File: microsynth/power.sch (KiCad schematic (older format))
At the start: 3 parts, among them J2 Conn_01x03_Male, J3 Conn_01x04_Male, J4 Conn_01x04_Male

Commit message: Add VCO2 on/off toggle, faceplace 3d, and new faceplate version
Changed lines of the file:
@@
 Wire Wire Line
 	4900 1500 4900 1350
-Text GLabel 5900 2900 2    50   BiDi ~ 0
+Text GLabel 5900 2600 2    50   BiDi ~ 0
 TRIG_IN_TO_SEQ_SKT
 Text GLabel 5900 2700 2    50   BiDi ~ 0
 VOUT_TO_SEQ_SKT
+Text GLabel 5900 2900 2    50   BiDi ~ 0
+VIN_TO_SEQ_SKT
 Text GLabel 5900 2800 2    50   BiDi ~ 0
-VIN_TO_SEQ_SKT
-Text GLabel 5900 2600 2    50   BiDi ~ 0
 TRIG_OUT_TO_SEQ_SKT
 Connection ~ 2250 1350

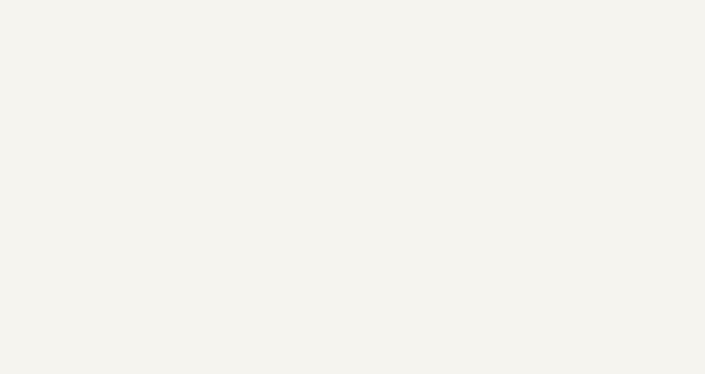
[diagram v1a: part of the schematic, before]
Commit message: Proper mounting holes
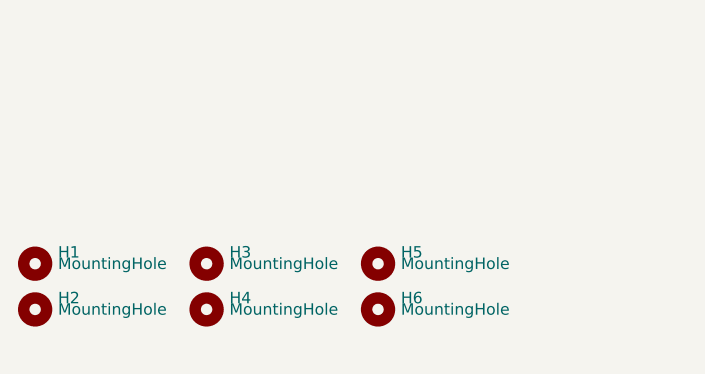
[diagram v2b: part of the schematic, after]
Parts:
- added H1, H2, H3, H4, H5, H6: MountingHole, MountingHole:MountingHole_3.2mm_M3, symbol Mechanical:MountingHole
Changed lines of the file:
@@
 Text GLabel 5900 3000 2    50   Input ~ 0
 VIN_FROM_SEQ
+$Comp
+L Mechanical:MountingHole H1
+U 1 1 5EBE889F
+P 1250 3300
+F 0 "H1" H 1350 3350 50  0000 L CNN
+F 1 "MountingHole" H 1350 3300 50  0000 L CNN
+F 2 "MountingHole:MountingHole_3.2mm_M3" H 1250 3300 50  0001 C CNN
+F 3 "~" H 1250 3300 50  0001 C CNN
+	1    1250 3300
+	1    0    0    -1
+$EndComp
+$Comp
+L Mechanical:MountingHole H2
+U 1 1 5EBEB2B9
+P 1250 3500
+F 0 "H2" H 1350 3550 50  0000 L CNN
+F 1 "MountingHole" H 1350 3500 50  0000 L CNN
+F 2 "MountingHole:MountingHole_3.2mm_M3" H 1250 3500 50  0001 C CNN
+F 3 "~" H 1250 3500 50  0001 C CNN
+	1    1250 3500
+	1    0    0    -1
+$EndComp
+$Comp
+L Mechanical:MountingHole H3
+U 1 1 5EBEC236
+P 2000 3300
+F 0 "H3" H 2100 3350 50  0000 L CNN
+F 1 "MountingHole" H 2100 3300 50  0000 L CNN
+F 2 "MountingHole:MountingHole_3.2mm_M3" H 2000 3300 50  0001 C CNN
+F 3 "~" H 2000 3300 50  0001 C CNN
+	1    2000 3300
+	1    0    0    -1
+$EndComp
+$Comp
+L Mechanical:MountingHole H4
+U 1 1 5EBEC23C
+P 2000 3500
+F 0 "H4" H 2100 3550 50  0000 L CNN
+F 1 "MountingHole" H 2100 3500 50  0000 L CNN
+F 2 "MountingHole:MountingHole_3.2mm_M3" H 2000 3500 50  0001 C CNN
+F 3 "~" H 2000 3500 50  0001 C CNN
+	1    2000 3500
+	1    0    0    -1
+$EndComp
+$Comp
+L Mechanical:MountingHole H5
+U 1 1 5EBECF2A
+P 2750 3300
+F 0 "H5" H 2850 3350 50  0000 L CNN
+F 1 "MountingHole" H 2850 3300 50  0000 L CNN
+F 2 "MountingHole:MountingHole_3.2mm_M3" H 2750 3300 50  0001 C CNN
+F 3 "~" H 2750 3300 50  0001 C CNN
+	1    2750 3300
+	1    0    0    -1
+$EndComp
+$Comp
+L Mechanical:MountingHole H6
+U 1 1 5EBECF30
+P 2750 3500
+F 0 "H6" H 2850 3550 50  0000 L CNN
+F 1 "MountingHole" H 2850 3500 50  0000 L CNN
+F 2 "MountingHole:MountingHole_3.2mm_M3" H 2750 3500 50  0001 C CNN
+F 3 "~" H 2750 3500 50  0001 C CNN
+	1    2750 3500
+	1    0    0    -1
+$EndComp
 $EndSCHEMATC

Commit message: Replace DP3T footprint, proper wire pads
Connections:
- net labels removed: +15V, -15V
- wire segments 10 -> 6
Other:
- moved on the sheet: J2
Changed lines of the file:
@@
 $EndDescr
-$Comp
-L power:+15V #PWR?
-U 1 1 5E05ECA4
-P 2500 1350
-F 0 "#PWR?" H 2500 1200 50  0001 C CNN
-F 1 "+15V" H 2515 1523 50  0000 C CNN
-F 2 "" H 2500 1350 50  0001 C CNN
-F 3 "" H 2500 1350 50  0001 C CNN
-	1    2500 1350
-	1    0    0    -1
-$EndComp
-$Comp
-L power:-15V #PWR?
-U 1 1 5E05F00D
-P 5450 1350
-F 0 "#PWR?" H 5450 1450 50  0001 C CNN
-F 1 "-15V" H 5465 1523 50  0000 C CNN
-F 2 "" H 5450 1350 50  0001 C CNN
-F 3 "" H 5450 1350 50  0001 C CNN
-	1    5450 1350
-	1    0    0    -1
-$EndComp
 $Comp
 L power:PWR_FLAG #FLG?
 U 1 1 5E0600E0
-P 2250 1350
-F 0 "#FLG?" H 2250 1425 50  0001 C CNN
-F 1 "PWR_FLAG" H 2250 1523 50  0000 C CNN
-F 2 "" H 2250 1350 50  0001 C CNN
-F 3 "~" H 2250 1350 50  0001 C CNN
-	1    2250 1350
-	1    0    0    -1
-$EndComp
-Wire Wire Line
-	4900 1350 5200 1350
+P 7450 1300
+F 0 "#FLG?" H 7450 1375 50  0001 C CNN
+F 1 "PWR_FLAG" H 7450 1473 50  0000 C CNN
+F 2 "" H 7450 1300 50  0001 C CNN
+F 3 "~" H 7450 1300 50  0001 C CNN
+	1    7450 1300
+	1    0    0    -1
+$EndComp
 $Comp
 L power:PWR_FLAG #FLG?
 U 1 1 5E0610BE
-P 5200 1350
-F 0 "#FLG?" H 5200 1425 50  0001 C CNN
-F 1 "PWR_FLAG" H 5200 1523 50  0000 C CNN
-F 2 "" H 5200 1350 50  0001 C CNN
-F 3 "~" H 5200 1350 50  0001 C CNN
-	1    5200 1350
-	1    0    0    -1
-$EndComp
-Connection ~ 5200 1350
-Wire Wire Line
-	5200 1350 5450 1350
+P 7150 1500
+F 0 "#FLG?" H 7150 1575 50  0001 C CNN
+F 1 "PWR_FLAG" H 7150 1673 50  0000 C CNN
+F 2 "" H 7150 1500 50  0001 C CNN
+F 3 "~" H 7150 1500 50  0001 C CNN
+	1    7150 1500
+	-1   0    0    1
+$EndComp
 $Comp
 L power:PWR_FLAG #FLG?
 U 1 1 5E061289
-P 3500 1350
-F 0 "#FLG?" H 3500 1425 50  0001 C CNN
-F 1 "PWR_FLAG" H 3500 1523 50  0000 C CNN
-F 2 "" H 3500 1350 50  0001 C CNN
-F 3 "~" H 3500 1350 50  0001 C CNN
-	1    3500 1350
-	1    0    0    -1
-$EndComp
-$Comp
-L power:GND #PWR?
-U 1 1 5E061374
-P 3700 1350
-F 0 "#PWR?" H 3700 1100 50  0001 C CNN
-F 1 "GND" H 3705 1177 50  0000 C CNN
-F 2 "" H 3700 1350 50  0001 C CNN
-F 3 "" H 3700 1350 50  0001 C CNN
-	1    3700 1350
-	1    0    0    -1
-$EndComp
-Wire Wire Line
-	3700 1350 3500 1350
-$Comp
-L power:+VSW #PWR?
-U 1 1 5E200EEA
-P 1950 1050
-F 0 "#PWR?" H 1950 900 50  0001 C CNN
-F 1 "+VSW" H 1965 1223 50  0000 C CNN
-F 2 "" H 1950 1050 50  0001 C CNN
-F 3 "" H 1950 1050 50  0001 C CNN
-	1    1950 1050
-	1    0    0    -1
-$EndComp
-Wire Wire Line
-	1950 1050 1950 1350
-$Comp
-L power:-VSW #PWR?
-U 1 1 5E201FCA
-P 4900 1500
-F 0 "#PWR?" H 4900 1600 50  0001 C CNN
-F 1 "-VSW" H 4915 1673 50  0000 C CNN
-F 2 "" H 4900 1500 50  0001 C CNN
-F 3 "" H 4900 1500 50  0001 C CNN
-	1    4900 1500
-	-1   0    0    1
-$EndComp
-Wire Wire Line
-	4900 1500 4900 1350
+P 7750 1400
+F 0 "#FLG?" H 7750 1475 50  0001 C CNN
+F 1 "PWR_FLAG" H 7750 1573 50  0000 C CNN
+F 2 "" H 7750 1400 50  0001 C CNN
+F 3 "~" H 7750 1400 50  0001 C CNN
+	1    7750 1400
+	1    0    0    -1
+$EndComp
 Text GLabel 5900 2600 2    50   BiDi ~ 0
 TRIG_IN_TO_SEQ_SKT
@@
 Text GLabel 5900 2800 2    50   BiDi ~ 0
 TRIG_OUT_TO_SEQ_SKT
-Connection ~ 2250 1350
-Wire Wire Line
-	2250 1350 2500 1350
-Wire Wire Line
-	1950 1350 2250 1350
 $Comp
 L Connector:Conn_01x03_Male J2
 U 1 1 5F1FC317
-P 5650 2100
-F 0 "J2" H 5800 2400 50  0000 C CNN
-F 1 "Conn_01x03_Male" H 5800 2300 50  0000 C CNN
-F 2 "Connector_PinHeader_2.54mm:PinHeader_1x03_P2.54mm_Vertical" H 5650 2100 50  0001 C CNN
-F 3 "~" H 5650 2100 50  0001 C CNN
-	1    5650 2100
+P 6500 1400
+F 0 "J2" H 6650 1700 50  0000 C CNN
+F 1 "Conn_01x03_Male" H 6650 1600 50  0000 C CNN
+F 2 "Connector_PinHeader_2.54mm:PinHeader_1x03_P2.54mm_Vertical" H 6500 1400 50  0001 C CNN
+F 3 "~" H 6500 1400 50  0001 C CNN
+	1    6500 1400
 	1    0    0    -1
 $EndComp
@@
 L power:-VSW #PWR?
 U 1 1 5F231D96
-P 6000 2200
-F 0 "#PWR?" H 6000 2300 50  0001 C CNN
-F 1 "-VSW" H 6015 2373 50  0000 C CNN
-F 2 "" H 6000 2200 50  0001 C CNN
-F 3 "" H 6000 2200 50  0001 C CNN
-	1    6000 2200
+P 6850 1500
+F 0 "#PWR?" H 6850 1600 50  0001 C CNN
+F 1 "-VSW" H 6865 1673 50  0000 C CNN
+F 2 "" H 6850 1500 50  0001 C CNN
+F 3 "" H 6850 1500 50  0001 C CNN
+	1    6850 1500
 	-1   0    0    1
 $EndComp
 Wire Wire Line
-	5850 2200 6000 2200
+	6700 1500 6850 1500
 $Comp
 L power:GND #PWR?
 U 1 1 5F232962
-P 6200 2100
-F 0 "#PWR?" H 6200 1850 50  0001 C CNN
-F 1 "GND" H 6205 1927 50  0000 C CNN
-F 2 "" H 6200 2100 50  0001 C CNN
-F 3 "" H 6200 2100 50  0001 C CNN
-	1    6200 2100
-	1    0    0    -1
-$EndComp
-Wire Wire Line
-	6200 2100 5850 2100
+P 7450 1400
+F 0 "#PWR?" H 7450 1150 50  0001 C CNN
+F 1 "GND" H 7455 1227 50  0000 C CNN
+F 2 "" H 7450 1400 50  0001 C CNN
+F 3 "" H 7450 1400 50  0001 C CNN
+	1    7450 1400
+	1    0    0    -1
+$EndComp
+Wire Wire Line
+	7450 1400 6700 1400
 $Comp
 L power:+VSW #PWR?
 U 1 1 5F233149
-P 6200 2000
-F 0 "#PWR?" H 6200 1850 50  0001 C CNN
-F 1 "+VSW" H 6215 2173 50  0000 C CNN
-F 2 "" H 6200 2000 50  0001 C CNN
-F 3 "" H 6200 2000 50  0001 C CNN
-	1    6200 2000
-	1    0    0    -1
-$EndComp
-Wire Wire Line
-	6200 2000 5850 2000
+P 7050 1300
+F 0 "#PWR?" H 7050 1150 50  0001 C CNN
+F 1 "+VSW" H 7065 1473 50  0000 C CNN
+F 2 "" H 7050 1300 50  0001 C CNN
+F 3 "" H 7050 1300 50  0001 C CNN
+	1    7050 1300
+	1    0    0    -1
+$EndComp
+Wire Wire Line
+	7050 1300 6700 1300
 Text GLabel 5900 3000 2    50   Input ~ 0
 VIN_FROM_SEQ
@@
 	1    0    0    -1
 $EndComp
+Wire Wire Line
+	7150 1500 6850 1500
+Connection ~ 6850 1500
+Wire Wire Line
+	7450 1300 7050 1300
+Connection ~ 7050 1300
+Wire Wire Line
+	7750 1400 7450 1400
+Connection ~ 7450 1400
 $EndSCHEMATC

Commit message: Add GND test point, add gnd to CV/Gate In/Out connector
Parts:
- added H9: MountingHole_Pad, Connector_PinHeader_2.54mm:PinHeader_1x01_P2.54mm_Vertical, symbol Mechanical:MountingHole_Pad
- J3: value Conn_01x04_Male -> Conn_01x06_Male; footprint Connector_PinHeader_2.54mm:PinHeader_1x05_P2.54mm_Vertical -> Connector_PinHeader_2.54mm:PinHeader_1x06_P2.54mm_Vertical; symbol Connector:Conn_01x05_Male -> Connector:Conn_01x06_Male
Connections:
- wire segments 6 -> 8
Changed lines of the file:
@@
-$EndComp
-$Comp
-L Connector:Conn_01x05_Male J3
-U 1 1 5F1FD92E
-P 5700 2800
-F 0 "J3" H 5700 3200 50  0000 C CNN
-F 1 "Conn_01x04_Male" H 6000 3100 50  0000 C CNN
-F 2 "Connector_PinHeader_2.54mm:PinHeader_1x05_P2.54mm_Vertical" H 5700 2800 50  0001 C CNN
-F 3 "~" H 5700 2800 50  0001 C CNN
-	1    5700 2800
-	1    0    0    -1
 $EndComp
 $Comp
@@
 	7750 1400 7450 1400
 Connection ~ 7450 1400
+$Comp
+L Mechanical:MountingHole_Pad H9
+U 1 1 5F3DC176
+P 2750 3750
+F 0 "H9" H 2850 3850 50  0000 L CNN
+F 1 "MountingHole_Pad" H 2850 3750 50  0000 L CNN
+F 2 "Connector_PinHeader_2.54mm:PinHeader_1x01_P2.54mm_Vertical" H 2750 3750 50  0001 C CNN
+F 3 "~" H 2750 3750 50  0001 C CNN
+	1    2750 3750
+	1    0    0    -1
+$EndComp
+$Comp
+L power:GND #PWR?
+U 1 1 5F3DCB17
+P 2750 3900
+F 0 "#PWR?" H 2750 3650 50  0001 C CNN
+F 1 "GND" H 2755 3727 50  0000 C CNN
+F 2 "" H 2750 3900 50  0001 C CNN
+F 3 "" H 2750 3900 50  0001 C CNN
+	1    2750 3900
+	1    0    0    -1
+$EndComp
+Wire Wire Line
+	2750 3900 2750 3850
+$Comp
+L Connector:Conn_01x06_Male J3
+U 1 1 5F1FD92E
+P 5700 2800
+F 0 "J3" H 5700 3200 50  0000 C CNN
+F 1 "Conn_01x06_Male" H 6000 3100 50  0000 C CNN
+F 2 "Connector_PinHeader_2.54mm:PinHeader_1x06_P2.54mm_Vertical" H 5700 2800 50  0001 C CNN
+F 3 "~" H 5700 2800 50  0001 C CNN
+	1    5700 2800
+	1    0    0    -1
+$EndComp
+$Comp
+L power:GND #PWR?
+U 1 1 5F3DEADD
+P 6850 3100
+F 0 "#PWR?" H 6850 2850 50  0001 C CNN
+F 1 "GND" H 6855 2927 50  0000 C CNN
+F 2 "" H 6850 3100 50  0001 C CNN
+F 3 "" H 6850 3100 50  0001 C CNN
+	1    6850 3100
+	1    0    0    -1
+$EndComp
+Wire Wire Line
+	6850 3100 5900 3100
 $EndSCHEMATC

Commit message: Annotate schematic
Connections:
- net +VSW renamed +9V
- net -VSW renamed -9V
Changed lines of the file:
@@
 L power:PWR_FLAG #FLG?
 U 1 1 5E0610BE
-P 7150 1500
-F 0 "#FLG?" H 7150 1575 50  0001 C CNN
-F 1 "PWR_FLAG" H 7150 1673 50  0000 C CNN
-F 2 "" H 7150 1500 50  0001 C CNN
-F 3 "~" H 7150 1500 50  0001 C CNN
-	1    7150 1500
+P 7450 1500
+F 0 "#FLG?" H 7450 1575 50  0001 C CNN
+F 1 "PWR_FLAG" H 7450 1673 50  0000 C CNN
+F 2 "" H 7450 1500 50  0001 C CNN
+F 3 "~" H 7450 1500 50  0001 C CNN
+	1    7450 1500
 	-1   0    0    1
 $EndComp
@@
 L power:PWR_FLAG #FLG?
 U 1 1 5E061289
-P 7750 1400
-F 0 "#FLG?" H 7750 1475 50  0001 C CNN
-F 1 "PWR_FLAG" H 7750 1573 50  0000 C CNN
-F 2 "" H 7750 1400 50  0001 C CNN
-F 3 "~" H 7750 1400 50  0001 C CNN
-	1    7750 1400
+P 8000 1400
+F 0 "#FLG?" H 8000 1475 50  0001 C CNN
+F 1 "PWR_FLAG" H 8000 1573 50  0000 C CNN
+F 2 "" H 8000 1400 50  0001 C CNN
+F 3 "~" H 8000 1400 50  0001 C CNN
+	1    8000 1400
 	1    0    0    -1
 $EndComp
@@
 L power:-VSW #PWR?
 U 1 1 5F231D96
-P 6850 1500
-F 0 "#PWR?" H 6850 1600 50  0001 C CNN
-F 1 "-VSW" H 6865 1673 50  0000 C CNN
-F 2 "" H 6850 1500 50  0001 C CNN
-F 3 "" H 6850 1500 50  0001 C CNN
-	1    6850 1500
+P 7050 1500
+F 0 "#PWR?" H 7050 1600 50  0001 C CNN
+F 1 "-VSW" H 7065 1673 50  0000 C CNN
+F 2 "" H 7050 1500 50  0001 C CNN
+F 3 "" H 7050 1500 50  0001 C CNN
+	1    7050 1500
 	-1   0    0    1
 $EndComp
 Wire Wire Line
-	6700 1500 6850 1500
+	6700 1500 7050 1500
 $Comp
 L power:GND #PWR?
 U 1 1 5F232962
-P 7450 1400
-F 0 "#PWR?" H 7450 1150 50  0001 C CNN
-F 1 "GND" H 7455 1227 50  0000 C CNN
-F 2 "" H 7450 1400 50  0001 C CNN
-F 3 "" H 7450 1400 50  0001 C CNN
-	1    7450 1400
-	1    0    0    -1
-$EndComp
-Wire Wire Line
-	7450 1400 6700 1400
+P 8000 1400
+F 0 "#PWR?" H 8000 1150 50  0001 C CNN
+F 1 "GND" H 8005 1227 50  0000 C CNN
+F 2 "" H 8000 1400 50  0001 C CNN
+F 3 "" H 8000 1400 50  0001 C CNN
+	1    8000 1400
+	1    0    0    -1
+$EndComp
+Wire Wire Line
+	8000 1400 6700 1400
 $Comp
 L power:+VSW #PWR?
@@
 $EndComp
 Wire Wire Line
-	7150 1500 6850 1500
-Connection ~ 6850 1500
+	7450 1500 7050 1500
+Connection ~ 7050 1500
 Wire Wire Line
 	7450 1300 7050 1300
 Connection ~ 7050 1300
-Wire Wire Line
-	7750 1400 7450 1400
-Connection ~ 7450 1400
+Connection ~ 8000 1400
 $Comp
 L Mechanical:MountingHole_Pad H9
@@
 Wire Wire Line
 	6850 3100 5900 3100
+$Comp
+L power:+9V #PWR?
+U 1 1 5F57157D
+P 7750 1300
+F 0 "#PWR?" H 7750 1150 50  0001 C CNN
+F 1 "+9V" H 7800 1500 50  0000 C CNN
+F 2 "" H 7750 1300 50  0001 C CNN
+F 3 "" H 7750 1300 50  0001 C CNN
+	1    7750 1300
+	1    0    0    -1
+$EndComp
+Wire Wire Line
+	7750 1300 7450 1300
+Connection ~ 7450 1300
+$Comp
+L power:-9V #PWR?
+U 1 1 5F572BDB
+P 7750 1500
+F 0 "#PWR?" H 7750 1375 50  0001 C CNN
+F 1 "-9V" H 7750 1700 50  0000 C CNN
+F 2 "" H 7750 1500 50  0001 C CNN
+F 3 "" H 7750 1500 50  0001 C CNN
+	1    7750 1500
+	-1   0    0    1
+$EndComp
+Wire Wire Line
+	7750 1500 7450 1500
+Connection ~ 7450 1500
 $EndSCHEMATC

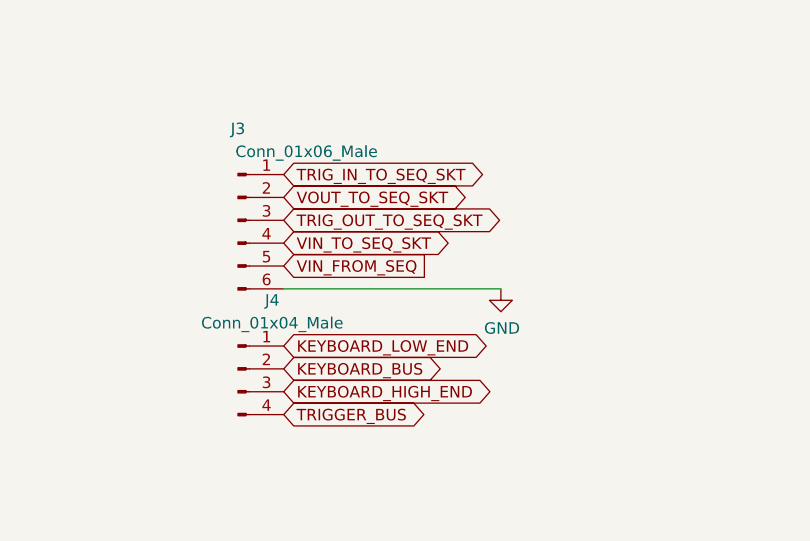
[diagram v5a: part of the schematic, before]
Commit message: Remove keyboard stuff
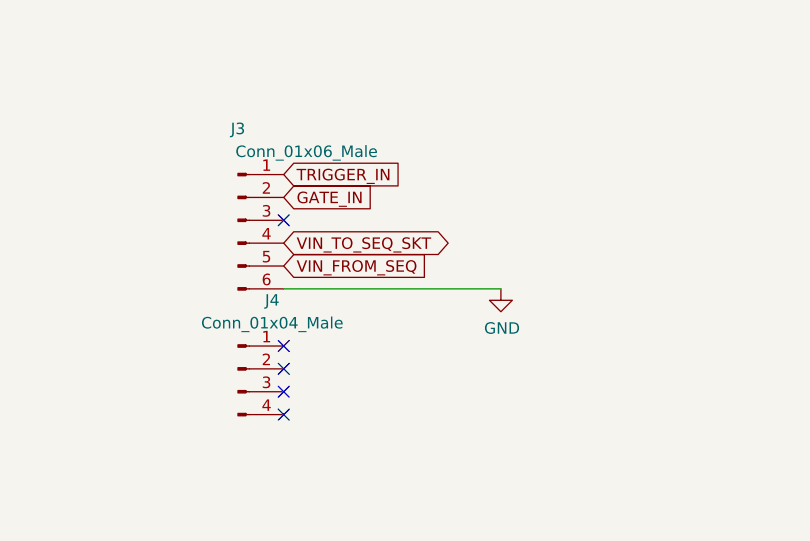
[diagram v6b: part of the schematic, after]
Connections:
- net KEYBOARD_BUS: no longer names the net of J4.2 (Pin_2)
- net KEYBOARD_HIGH_END: no longer names the net of J4.3 (Pin_3)
- net KEYBOARD_LOW_END: no longer names the net of J4.1 (Pin_1)
- net TRIGGER_BUS: no longer names the net of J4.4 (Pin_4)
- net TRIG_IN_TO_SEQ_SKT renamed TRIGGER_IN
- net TRIG_OUT_TO_SEQ_SKT: no longer names the net of J3.3 (Pin_3)
- net VOUT_TO_SEQ_SKT renamed GATE_IN
- no-connect marks 0 -> 5
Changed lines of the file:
@@
 	1    0    0    -1
 $EndComp
-Text GLabel 5900 2600 2    50   BiDi ~ 0
-TRIG_IN_TO_SEQ_SKT
-Text GLabel 5900 2700 2    50   BiDi ~ 0
-VOUT_TO_SEQ_SKT
+Text GLabel 5900 2600 2    50   Input ~ 0
+TRIGGER_IN
 Text GLabel 5900 2900 2    50   BiDi ~ 0
 VIN_TO_SEQ_SKT
-Text GLabel 5900 2800 2    50   BiDi ~ 0
-TRIG_OUT_TO_SEQ_SKT
 $Comp
 L Connector:Conn_01x03_Male J2
@@
 	1    0    0    -1
 $EndComp
-Text GLabel 5900 3550 2    50   BiDi ~ 0
-KEYBOARD_HIGH_END
-Text GLabel 5900 3350 2    50   BiDi ~ 0
-KEYBOARD_LOW_END
-Text GLabel 5900 3450 2    50   BiDi ~ 0
-KEYBOARD_BUS
-Text GLabel 5900 3650 2    50   BiDi ~ 0
-TRIGGER_BUS
 $Comp
 L power:-VSW #PWR?
@@
 	7750 1500 7450 1500
 Connection ~ 7450 1500
+NoConn ~ 5900 3350
+NoConn ~ 5900 3450
+NoConn ~ 5900 3550
+NoConn ~ 5900 3650
+NoConn ~ 5900 2800
+Text GLabel 5900 2700 2    50   Input ~ 0
+GATE_IN
 $EndSCHEMATC

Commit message: Clean up and reroute
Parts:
- removed J4: Conn_01x04_Male, Connector_PinHeader_2.54mm:PinHeader_1x04_P2.54mm_Vertical, symbol Connector:Conn_01x04_Male
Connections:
- net VIN_FROM_SEQ renamed CV_IN
- net VIN_TO_SEQ_SKT renamed CV_IN_2
- no-connect marks 5 -> 1
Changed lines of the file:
@@
 Text GLabel 5900 2600 2    50   Input ~ 0
 TRIGGER_IN
-Text GLabel 5900 2900 2    50   BiDi ~ 0
-VIN_TO_SEQ_SKT
+Text GLabel 5900 3000 2    50   Input ~ 0
+CV_IN
 $Comp
 L Connector:Conn_01x03_Male J2
@@
 F 3 "~" H 6500 1400 50  0001 C CNN
 	1    6500 1400
-	1    0    0    -1
-$EndComp
-$Comp
-L Connector:Conn_01x04_Male J4
-U 1 1 5F1FE242
-P 5700 3450
-F 0 "J4" H 5850 3750 50  0000 C CNN
-F 1 "Conn_01x04_Male" H 5850 3650 50  0000 C CNN
-F 2 "Connector_PinHeader_2.54mm:PinHeader_1x04_P2.54mm_Vertical" H 5700 3450 50  0001 C CNN
-F 3 "~" H 5700 3450 50  0001 C CNN
-	1    5700 3450
 	1    0    0    -1
 $EndComp
@@
 Wire Wire Line
 	7050 1300 6700 1300
-Text GLabel 5900 3000 2    50   Input ~ 0
-VIN_FROM_SEQ
+Text GLabel 5900 2900 2    50   Input ~ 0
+CV_IN_2
 $Comp
 L Mechanical:MountingHole H1
@@
 	7750 1500 7450 1500
 Connection ~ 7450 1500
-NoConn ~ 5900 3350
-NoConn ~ 5900 3450
-NoConn ~ 5900 3550
-NoConn ~ 5900 3650
 NoConn ~ 5900 2800
 Text GLabel 5900 2700 2    50   Input ~ 0
